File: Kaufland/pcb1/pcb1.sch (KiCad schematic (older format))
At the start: 9 parts

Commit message: First pcb model (to be fixed)
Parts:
- added R3: 4.7k, Resistor_THT:R_Axial_DIN0204_L3.6mm_D1.6mm_P1.90mm_Vertical, symbol Device:R
- added SW1: SW_Push, Connector_PinHeader_2.54mm:PinHeader_1x02_P2.54mm_Vertical, symbol Switch:SW_Push
- D1: renamed from D?; footprint (none) -> Diode_THT:D_A-405_P5.08mm_Vertical_KathodeUp
- D2: renamed from D?; footprint (none) -> Diode_THT:D_DO-15_P5.08mm_Vertical_KathodeUp
- J1: renamed from J?; footprint (none) -> Connector_Audio:Jack_3.5mm_PJ320D_Horizontal
- J2: renamed from J?; footprint (none) -> Connector_BarrelJack:BarrelJack_CUI_PJ-063AH_Horizontal
- R1: renamed from R?; footprint (none) -> Resistor_THT:R_Axial_DIN0204_L3.6mm_D1.6mm_P1.90mm_Vertical
- R2: renamed from R?; value 1k -> 330; footprint (none) -> Resistor_THT:R_Axial_DIN0204_L3.6mm_D1.6mm_P1.90mm_Vertical
- U1: renamed from U?; footprint (none) -> pcb1:DFPlayerMini; symbol My_Library:DF_Player -> pcb1-rescue:DF_Player-My_Library
- U2: renamed from U?; footprint (none) -> Connector_PinHeader_2.54mm:PinHeader_1x04_P2.54mm_Vertical; symbol My_Library:RGB_LED_STRIP -> pcb1-rescue:RGB_LED_STRIP-My_Library
- gave numbers to parts that had none: 1
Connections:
- net labels removed: GND
- wire segments 44 -> 48
- no-connect marks 30 -> 29
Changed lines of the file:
@@
 $EndDescr
 $Comp
-L Connector:AudioJack2 J?
+L Connector:AudioJack2 J1
 U 1 1 5F31EC30
 P 3750 2300
-F 0 "J?" H 3782 2625 50  0000 C CNN
+F 0 "J1" H 3782 2625 50  0000 C CNN
 F 1 "AudioJack2" H 3782 2534 50  0000 C CNN
-F 2 "" H 3750 2300 50  0001 C CNN
+F 2 "Connector_Audio:Jack_3.5mm_PJ320D_Horizontal" H 3750 2300 50  0001 C CNN
 F 3 "~" H 3750 2300 50  0001 C CNN
 	1    3750 2300
@@
 	3250 2300 3550 2300
 $Comp
-L My_Library:DF_Player U?
+L pcb1-rescue:DF_Player-My_Library U1
 U 1 1 5F31DE61
 P 2550 3400
-F 0 "U?" H 2525 3365 50  0000 C CNN
+F 0 "U1" H 2525 3365 50  0000 C CNN
 F 1 "DF_Player" H 2525 3274 50  0000 C CNN
-F 2 "" H 2300 3250 50  0001 C CNN
+F 2 "pcb1:DFPlayerMini" H 2300 3250 50  0001 C CNN
 F 3 "" H 2300 3250 50  0001 C CNN
 	1    2550 3400
@@
 NoConn ~ 5100 3400
 NoConn ~ 5100 3500
-NoConn ~ 5100 3600
 NoConn ~ 5100 3700
 NoConn ~ 5100 4100
@@
 NoConn ~ 6100 2900
 $Comp
-L Device:R R?
+L Device:R R1
 U 1 1 5F332E0C
 P 3550 3000
-F 0 "R?" V 3343 3000 50  0000 C CNN
+F 0 "R1" V 3343 3000 50  0000 C CNN
 F 1 "1k" V 3434 3000 50  0000 C CNN
-F 2 "" V 3480 3000 50  0001 C CNN
+F 2 "Resistor_THT:R_Axial_DIN0204_L3.6mm_D1.6mm_P1.90mm_Vertical" V 3480 3000 50  0001 C CNN
 F 3 "~" H 3550 3000 50  0001 C CNN
 	1    3550 3000
@@
 	1    0    0    -1
 $EndComp
-$Comp
-L power:GND #PWR0104
-U 1 1 5F33866E
-P 6850 2550
-F 0 "#PWR0104" H 6850 2300 50  0001 C CNN
-F 1 "GND" H 6855 2377 50  0000 C CNN
-F 2 "" H 6850 2550 50  0001 C CNN
-F 3 "" H 6850 2550 50  0001 C CNN
-	1    6850 2550
-	1    0    0    -1
-$EndComp
 Wire Wire Line
 	5600 4600 5600 4900
 $Comp
-L Connector:Barrel_Jack J?
+L Connector:Barrel_Jack J2
 U 1 1 5F33FB12
 P 6400 2450
-F 0 "J?" H 6457 2775 50  0000 C CNN
+F 0 "J2" H 6457 2775 50  0000 C CNN
 F 1 "Barrel_Jack" H 6457 2684 50  0000 C CNN
-F 2 "" H 6450 2410 50  0001 C CNN
+F 2 "Connector_BarrelJack:BarrelJack_CUI_PJ-063AH_Horizontal" H 6450 2410 50  0001 C CNN
 F 3 "~" H 6450 2410 50  0001 C CNN
 	1    6400 2450
@@
 	3150 1950 3150 3100
 $Comp
-L My_Library:RGB_LED_STRIP U?
+L pcb1-rescue:RGB_LED_STRIP-My_Library U2
 U 1 1 5F34A31E
 P 4050 4450
-F 0 "U?" H 4528 4146 50  0000 L CNN
+F 0 "U2" H 4528 4146 50  0000 L CNN
 F 1 "RGB_LED_STRIP" H 4528 4055 50  0000 L CNN
-F 2 "" H 4050 4450 50  0001 C CNN
+F 2 "Connector_PinHeader_2.54mm:PinHeader_1x04_P2.54mm_Vertical" H 4050 4450 50  0001 C CNN
 F 3 "" H 4050 4450 50  0001 C CNN
 	1    4050 4450
@@
 	3900 4400 3900 4650
 $Comp
-L power:+12V #PWR?
+L power:+12V #PWR06
 U 1 1 5F350095
 P 6700 2100
-F 0 "#PWR?" H 6700 1950 50  0001 C CNN
+F 0 "#PWR06" H 6700 1950 50  0001 C CNN
 F 1 "+12V" H 6715 2273 50  0000 C CNN
 F 2 "" H 6700 2100 50  0001 C CNN
@@
 	6700 2100 6700 2350
 $Comp
-L power:+12V #PWR?
+L power:+12V #PWR03
 U 1 1 5F35227C
 P 5500 1900
-F 0 "#PWR?" H 5500 1750 50  0001 C CNN
+F 0 "#PWR03" H 5500 1750 50  0001 C CNN
 F 1 "+12V" H 5515 2073 50  0000 C CNN
 F 2 "" H 5500 1900 50  0001 C CNN
@@
 	5500 1900 5500 2500
 $Comp
-L power:+5V #PWR?
+L power:+5V #PWR05
 U 1 1 5F35321B
 P 5800 1900
-F 0 "#PWR?" H 5800 1750 50  0001 C CNN
+F 0 "#PWR05" H 5800 1750 50  0001 C CNN
 F 1 "+5V" H 5815 2073 50  0000 C CNN
 F 2 "" H 5800 1900 50  0001 C CNN
@@
 $EndComp
 $Comp
-L power:+5V #PWR?
+L power:+5V #PWR01
 U 1 1 5F353E00
 P 3150 1950
-F 0 "#PWR?" H 3150 1800 50  0001 C CNN
+F 0 "#PWR01" H 3150 1800 50  0001 C CNN
 F 1 "+5V" H 3165 2123 50  0000 C CNN
 F 2 "" H 3150 1950 50  0001 C CNN
@@
 	4900 3200 4900 3600
 $Comp
-L MCU_Module:Arduino_UNO_R3 A?
+L MCU_Module:Arduino_UNO_R3 A1
 U 1 1 5F31A11A
 P 5600 3500
-F 0 "A?" H 5600 4681 50  0000 C CNN
+F 0 "A1" H 5600 4681 50  0000 C CNN
 F 1 "Arduino_UNO_R3" H 5600 4590 50  0000 C CNN
 F 2 "Module:Arduino_UNO_R3" H 5600 3500 50  0001 C CIN
@@
 $EndComp
 $Comp
-L Device:R R?
+L Device:R R2
 U 1 1 5F366658
 P 4500 3100
-F 0 "R?" V 4293 3100 50  0000 C CNN
-F 1 "1k" V 4384 3100 50  0000 C CNN
-F 2 "" V 4430 3100 50  0001 C CNN
+F 0 "R2" V 4293 3100 50  0000 C CNN
+F 1 "330" V 4384 3100 50  0000 C CNN
+F 2 "Resistor_THT:R_Axial_DIN0204_L3.6mm_D1.6mm_P1.90mm_Vertical" V 4430 3100 50  0001 C CNN
 F 3 "~" H 4500 3100 50  0001 C CNN
 	1    4500 3100
@@
 	3850 3200 4100 3200
 $Comp
-L Device:LED D?
+L Device:LED D2
 U 1 1 5F362957
 P 4350 3350
-F 0 "D?" V 4297 3428 50  0000 L CNN
+F 0 "D2" V 4297 3428 50  0000 L CNN
 F 1 "LED" V 4388 3428 50  0000 L CNN
-F 2 "" H 4350 3350 50  0001 C CNN
+F 2 "Diode_THT:D_DO-15_P5.08mm_Vertical_KathodeUp" H 4350 3350 50  0001 C CNN
 F 3 "~" H 4350 3350 50  0001 C CNN
 	1    4350 3350
@@
 $EndComp
 $Comp
-L Device:LED D?
+L Device:LED D1
 U 1 1 5F36176B
 P 3850 3350
-F 0 "D?" V 3797 3428 50  0000 L CNN
+F 0 "D1" V 3797 3428 50  0000 L CNN
 F 1 "LED" V 3888 3428 50  0000 L CNN
-F 2 "" H 3850 3350 50  0001 C CNN
+F 2 "Diode_THT:D_A-405_P5.08mm_Vertical_KathodeUp" H 3850 3350 50  0001 C CNN
 F 3 "~" H 3850 3350 50  0001 C CNN
 	1    3850 3350
@@
 Wire Wire Line
 	4100 3600 4900 3600
+$Comp
+L Device:R R3
+U 1 1 5F31CE82
+P 5000 5750
+F 0 "R3" H 5070 5796 50  0000 L CNN
+F 1 "4.7k" H 5070 5705 50  0000 L CNN
+F 2 "Resistor_THT:R_Axial_DIN0204_L3.6mm_D1.6mm_P1.90mm_Vertical" V 4930 5750 50  0001 C CNN
+F 3 "~" H 5000 5750 50  0001 C CNN
+	1    5000 5750
+	1    0    0    -1
+$EndComp
+$Comp
+L power:+5V #PWR04
+U 1 1 5F31F7F6
+P 5600 5500
+F 0 "#PWR04" H 5600 5350 50  0001 C CNN
+F 1 "+5V" H 5615 5673 50  0000 C CNN
+F 2 "" H 5600 5500 50  0001 C CNN
+F 3 "" H 5600 5500 50  0001 C CNN
+	1    5600 5500
+	1    0    0    -1
+$EndComp
+Wire Wire Line
+	5000 3600 5100 3600
+$Comp
+L power:GNDREF #PWR07
+U 1 1 5F33A6D0
+P 6850 2550
+F 0 "#PWR07" H 6850 2300 50  0001 C CNN
+F 1 "GNDREF" H 6855 2377 50  0000 C CNN
+F 2 "" H 6850 2550 50  0001 C CNN
+F 3 "" H 6850 2550 50  0001 C CNN
+	1    6850 2550
+	1    0    0    -1
+$EndComp
+$Comp
+L power:GNDREF #PWR02
+U 1 1 5F33CA2D
+P 5000 5900
+F 0 "#PWR02" H 5000 5650 50  0001 C CNN
+F 1 "GNDREF" H 5005 5727 50  0000 C CNN
+F 2 "" H 5000 5900 50  0001 C CNN
+F 3 "" H 5000 5900 50  0001 C CNN
+	1    5000 5900
+	1    0    0    -1
+$EndComp
+Wire Wire Line
+	5400 5500 5600 5500
+Wire Wire Line
+	5000 3600 5000 5500
+$Comp
+L Switch:SW_Push SW1
+U 1 1 5F35F458
+P 5200 5500
+F 0 "SW1" H 5200 5785 50  0000 C CNN
+F 1 "SW_Push" H 5200 5694 50  0000 C CNN
+F 2 "Connector_PinHeader_2.54mm:PinHeader_1x02_P2.54mm_Vertical" H 5200 5700 50  0001 C CNN
+F 3 "~" H 5200 5700 50  0001 C CNN
+	1    5200 5500
+	1    0    0    -1
+$EndComp
+Connection ~ 5000 5500
+Wire Wire Line
+	5000 5500 5000 5600
 $EndSCHEMATC

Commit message: Flipped pcb (to be checked; routed)
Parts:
- D2: footprint Diode_THT:D_DO-15_P5.08mm_Vertical_KathodeUp -> Diode_THT:D_A-405_P5.08mm_Vertical_KathodeUp
- J1: footprint Connector_Audio:Jack_3.5mm_PJ320D_Horizontal -> Connector_Audio:Jack_3.5mm_PJ320E_Horizontal
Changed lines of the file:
@@
 F 0 "J1" H 3782 2625 50  0000 C CNN
 F 1 "AudioJack2" H 3782 2534 50  0000 C CNN
-F 2 "Connector_Audio:Jack_3.5mm_PJ320D_Horizontal" H 3750 2300 50  0001 C CNN
+F 2 "Connector_Audio:Jack_3.5mm_PJ320E_Horizontal" H 3750 2300 50  0001 C CNN
 F 3 "~" H 3750 2300 50  0001 C CNN
 	1    3750 2300
@@
 F 0 "D2" V 4297 3428 50  0000 L CNN
 F 1 "LED" V 4388 3428 50  0000 L CNN
-F 2 "Diode_THT:D_DO-15_P5.08mm_Vertical_KathodeUp" H 4350 3350 50  0001 C CNN
+F 2 "Diode_THT:D_A-405_P5.08mm_Vertical_KathodeUp" H 4350 3350 50  0001 C CNN
 F 3 "~" H 4350 3350 50  0001 C CNN
 	1    4350 3350

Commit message: small changes to the pcb
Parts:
- R1, R2, R3: footprint Resistor_THT:R_Axial_DIN0204_L3.6mm_D1.6mm_P1.90mm_Vertical -> Resistor_THT:R_Axial_DIN0204_L3.6mm_D1.6mm_P7.62mm_Horizontal
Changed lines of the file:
@@
 F 0 "R1" V 3343 3000 50  0000 C CNN
 F 1 "1k" V 3434 3000 50  0000 C CNN
-F 2 "Resistor_THT:R_Axial_DIN0204_L3.6mm_D1.6mm_P1.90mm_Vertical" V 3480 3000 50  0001 C CNN
+F 2 "Resistor_THT:R_Axial_DIN0204_L3.6mm_D1.6mm_P7.62mm_Horizontal" V 3480 3000 50  0001 C CNN
 F 3 "~" H 3550 3000 50  0001 C CNN
 	1    3550 3000
@@
 F 0 "R2" V 4293 3100 50  0000 C CNN
 F 1 "330" V 4384 3100 50  0000 C CNN
-F 2 "Resistor_THT:R_Axial_DIN0204_L3.6mm_D1.6mm_P1.90mm_Vertical" V 4430 3100 50  0001 C CNN
+F 2 "Resistor_THT:R_Axial_DIN0204_L3.6mm_D1.6mm_P7.62mm_Horizontal" V 4430 3100 50  0001 C CNN
 F 3 "~" H 4500 3100 50  0001 C CNN
 	1    4500 3100
@@
 F 0 "R3" H 5070 5796 50  0000 L CNN
 F 1 "4.7k" H 5070 5705 50  0000 L CNN
-F 2 "Resistor_THT:R_Axial_DIN0204_L3.6mm_D1.6mm_P1.90mm_Vertical" V 4930 5750 50  0001 C CNN
+F 2 "Resistor_THT:R_Axial_DIN0204_L3.6mm_D1.6mm_P7.62mm_Horizontal" V 4930 5750 50  0001 C CNN
 F 3 "~" H 5000 5750 50  0001 C CNN
 	1    5000 5750

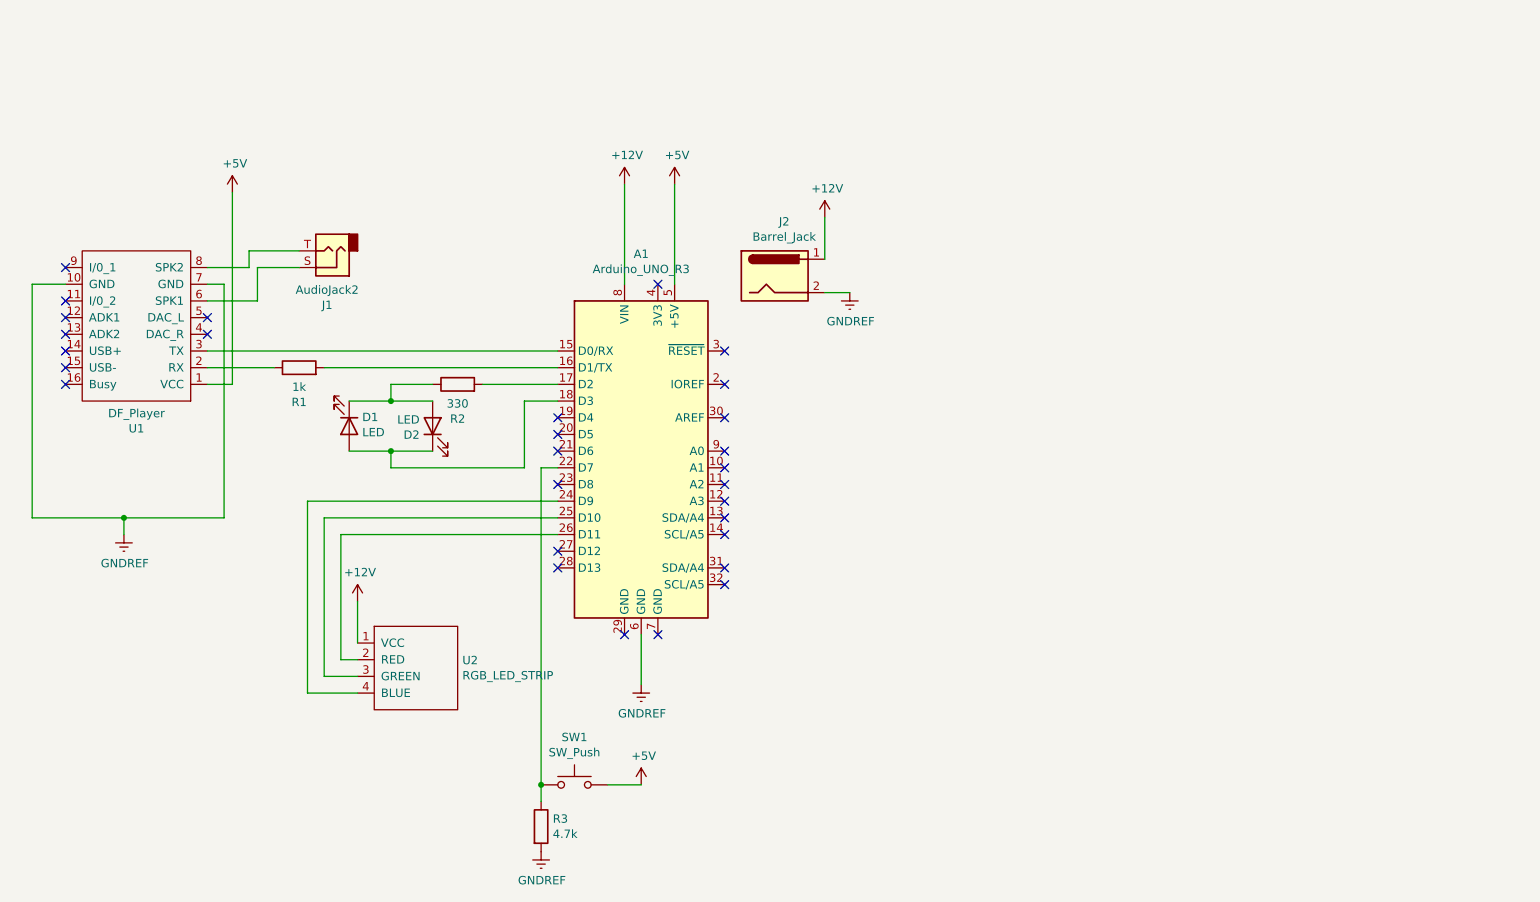
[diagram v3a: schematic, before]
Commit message: added additional strip 2 more leds and a button to pcb
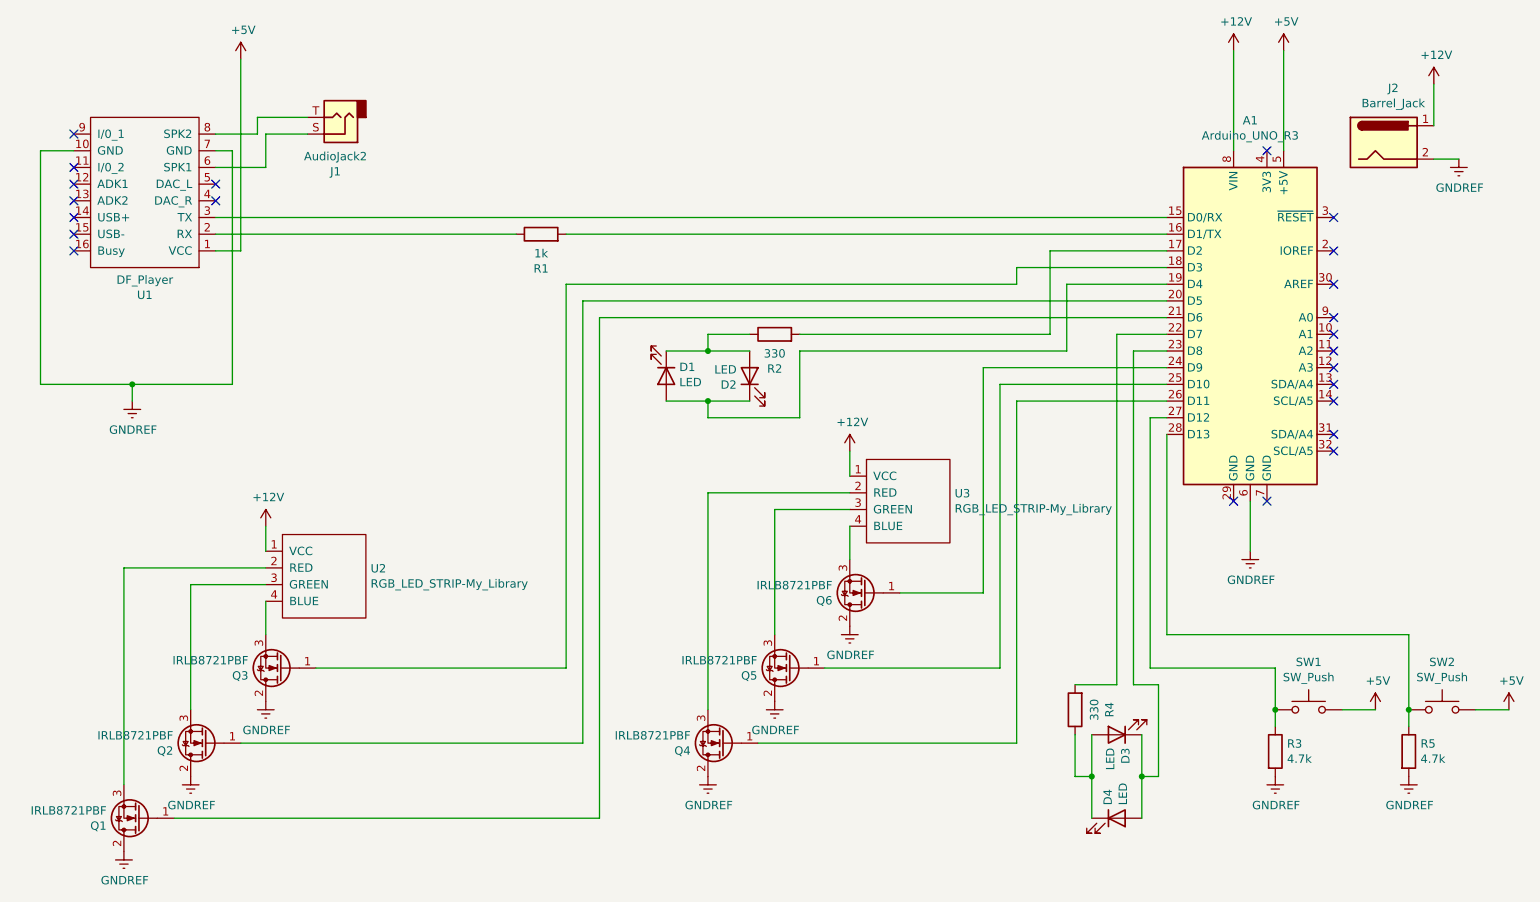
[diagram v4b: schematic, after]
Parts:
- added D3, D4: LED, Connector:FanPinHeader_1x03_P2.54mm_Vertical, symbol Device:LED
- added Q1, Q2, Q3, Q4, Q5, Q6: IRLB8721PBF, Package_TO_SOT_THT:TO-220-3_Vertical, symbol Transistor_FET:IRLB8721PBF
- added R4: 330, Resistor_THT:R_Axial_DIN0204_L3.6mm_D1.6mm_P7.62mm_Horizontal, symbol Device:R
- added R5: 4.7k, Resistor_THT:R_Axial_DIN0204_L3.6mm_D1.6mm_P7.62mm_Horizontal, symbol Device:R
- added SW2: SW_Push, Connector:FanPinHeader_1x03_P2.54mm_Vertical, symbol Switch:SW_Push
- added U3: RGB_LED_STRIP-My_Library, Connector:FanPinHeader_1x04_P2.54mm_Vertical, symbol pcb1-rescue:RGB_LED_STRIP-My_Library
- D1, D2: footprint Diode_THT:D_A-405_P5.08mm_Vertical_KathodeUp -> Connector:FanPinHeader_1x03_P2.54mm_Vertical
- SW1: footprint Connector_PinHeader_2.54mm:PinHeader_1x02_P2.54mm_Vertical -> Connector:FanPinHeader_1x03_P2.54mm_Vertical
- U2: value RGB_LED_STRIP -> RGB_LED_STRIP-My_Library; footprint Connector_PinHeader_2.54mm:PinHeader_1x04_P2.54mm_Vertical -> Connector:FanPinHeader_1x04_P2.54mm_Vertical
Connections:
- net +12V: now also U3.1 (VCC)
- net +5V: now also SW2.2
- net GNDREF: now also Q1.2 (D), Q2.2 (D), Q3.2 (D), Q4.2 (D), Q5.2 (D), Q6.2 (D), R5.2
- net at D1.2 (A), D2.1 (K): now also A1.19 (D4); no longer A1.18 (D3)
- net at A1.20 (D5): now also Q2.1 (G)
- net at A1.21 (D6): now also Q1.1 (G)
- net at R3.1, SW1.1: now also A1.27 (D12); no longer A1.22 (D7)
- net at A1.23 (D8): now also D3.1 (K), D4.2 (A)
- net at A1.24 (D9): now also Q6.1 (G); no longer U2.4 (BLUE)
- net at A1.25 (D10): now also Q5.1 (G); no longer U2.3 (GREEN)
- net at A1.26 (D11): now also Q4.1 (G); no longer U2.2 (RED)
- net at A1.28 (D13): now also R5.1, SW2.1
- new net: A1.18 (D3), Q3.1 (G)
- new net: A1.22 (D7), R4.2
- new net: Q1.3 (S), U2.2 (RED)
- new net: Q2.3 (S), U2.3 (GREEN)
- new net: Q3.3 (S), U2.4 (BLUE)
- new net: D3.2 (A), D4.1 (K), R4.1
- new net: Q4.3 (S), U3.2 (RED)
- new net: Q5.3 (S), U3.3 (GREEN)
- new net: Q6.3 (S), U3.4 (BLUE)
- no-connect marks 29 -> 23
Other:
- moved on the sheet: A1, D1, D2, J1, J2, R1, R2, R3, SW1, U1

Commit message: Changed pins for LED strips
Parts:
- U2, U3: footprint Connector:FanPinHeader_1x04_P2.54mm_Vertical -> Connector_JST:JST_EH_S4B-EH_1x04_P2.50mm_Horizontal
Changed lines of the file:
@@
 F 0 "U2" H 3978 3596 50  0000 L CNN
 F 1 "RGB_LED_STRIP-My_Library" H 3978 3505 50  0000 L CNN
-F 2 "Connector:FanPinHeader_1x04_P2.54mm_Vertical" H 3500 3900 50  0001 C CNN
+F 2 "Connector_JST:JST_EH_S4B-EH_1x04_P2.50mm_Horizontal" H 3500 3900 50  0001 C CNN
 F 3 "" H 3500 3900 50  0001 C CNN
 	1    3500 3900
@@
 F 0 "U3" H 7478 3146 50  0000 L CNN
 F 1 "RGB_LED_STRIP-My_Library" H 7478 3055 50  0000 L CNN
-F 2 "Connector:FanPinHeader_1x04_P2.54mm_Vertical" H 7000 3450 50  0001 C CNN
+F 2 "Connector_JST:JST_EH_S4B-EH_1x04_P2.50mm_Horizontal" H 7000 3450 50  0001 C CNN
 F 3 "" H 7000 3450 50  0001 C CNN
 	1    7000 3450
